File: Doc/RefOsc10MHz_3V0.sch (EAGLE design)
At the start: 54 parts, among them CON1 MCX-J-P-X-RA-SM1, CON2 TYCO-AMP_USBUSB-B_SMT, CON3 SD-73100-0105, CON4 AVR-ISP-6SMD, CON5 AVR-JTAG-10SMD, CON6 HEADER-2X3SMD, CON7 MCX-J-P-X-RA-SM1, IC11 712-RXM-GNSS-TM-B, IC3 74HCT221D, IC4 CFPT-141

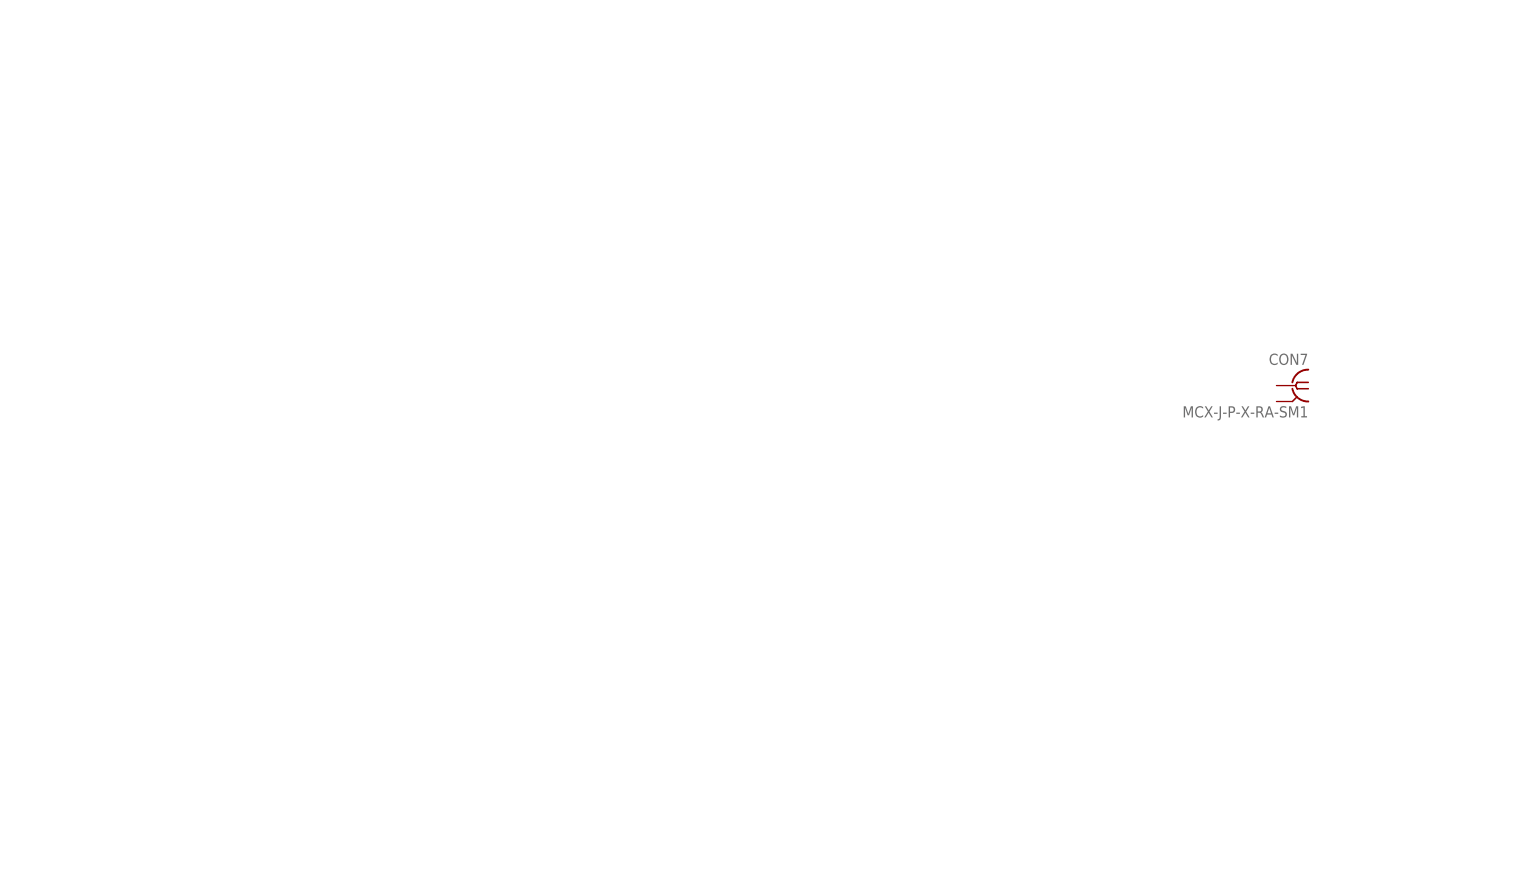
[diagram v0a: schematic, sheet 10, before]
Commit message: avr_DF4IAH_Bootloader - Doc - Eagle: V3.0 - REAR panel connected
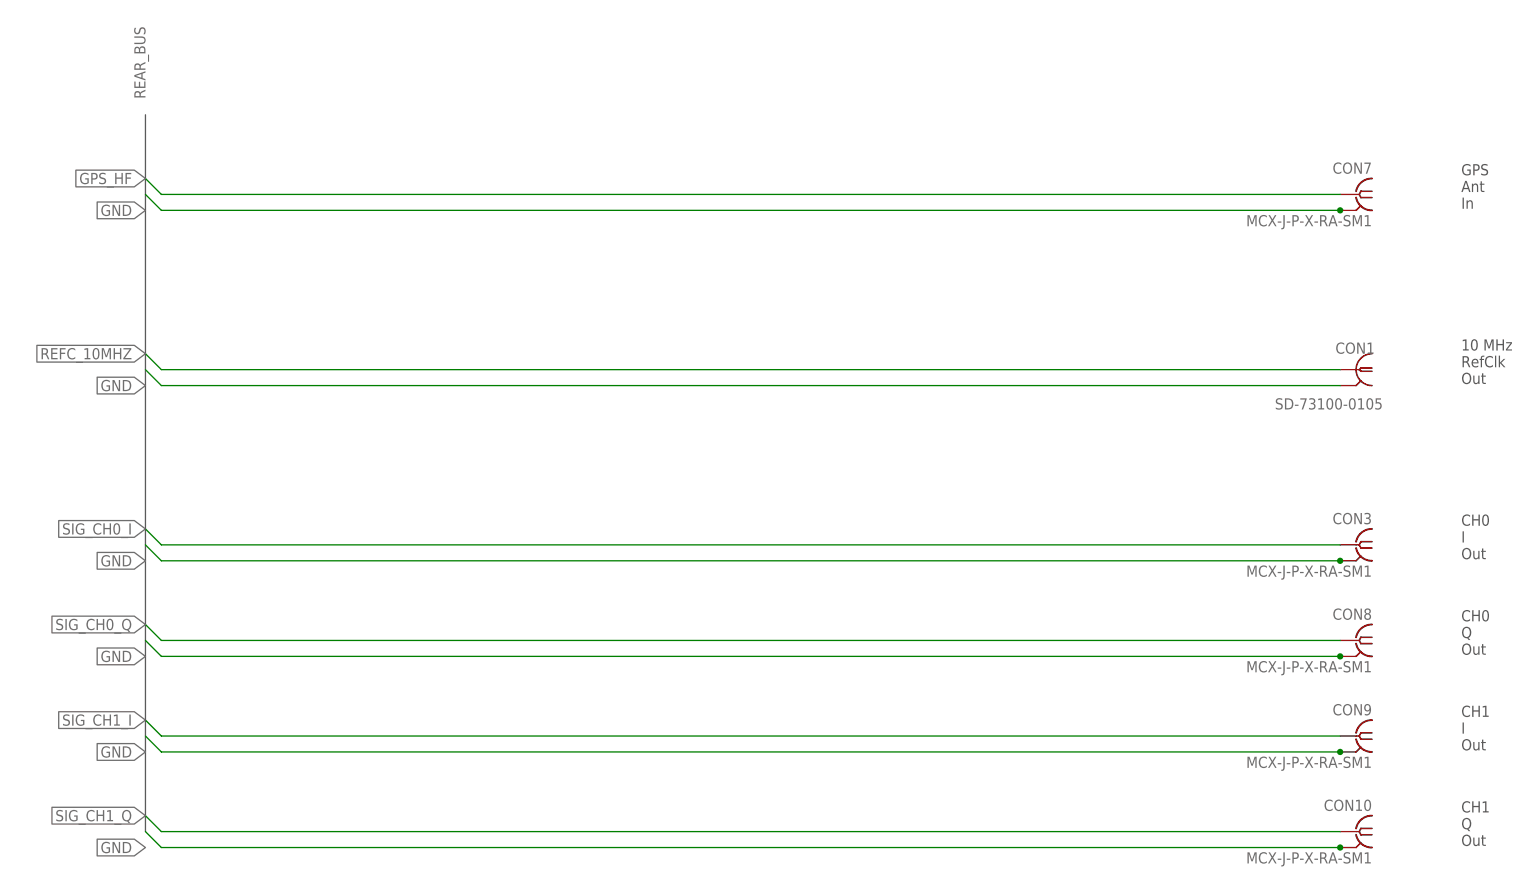
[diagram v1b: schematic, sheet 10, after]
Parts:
- removed R61: 51, rcl:R-EU_R0805
- added CON10, CON8, CON9: MCX-J-P-X-RA-SM1, df4iah:MCX-J-P-X-RA-SM1
- added R10: 51, rcl:R-EU_R0805
- CON1: value MCX-J-P-X-RA-SM1 -> SD-73100-0105; device df4iah:MCX-J-P-X-RA-SM1 -> df4iah:MOLEX_BNC-JACK-50R_SD-73100-0105
- CON3: value SD-73100-0105 -> MCX-J-P-X-RA-SM1; device df4iah:MOLEX_BNC-JACK-50R_SD-73100-0105 -> df4iah:MCX-J-P-X-RA-SM1
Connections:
- removed net C_10MHZ: R61.1
- removed net N$42: CON3.1, R61.2
- new net REFC_10MHZ: CON1.1
- new net SIG_CH0_I: CON3.1
- new net SIG_CH0_Q: CON8.1
- new net SIG_CH1_I: CON9.1
- new net SIG_CH1_Q: CON10.1
- net GND: now also CON1.2, CON1.3, CON10.2, CON10.3, CON10.4, CON10.5, CON3.4, CON3.5, CON7.2, CON7.3, CON7.4, CON7.5, CON8.2, CON8.3, CON8.4, CON8.5, CON9.2, CON9.3, CON9.4, CON9.5
- net GPS_HF: now also CON7.1
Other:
- note added: "CH0 I Out"
- note added: "CH0 Q Out"
- note added: "CH1 I Out"
- note added: "CH1 Q Out"
- note added: "GPS Ant In"
- moved on the sheet: CON7

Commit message: avr_DF4IAH_Bootloader - Doc - Eagle: V3.0 - FPGA and MMU, first attempt, added
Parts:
- added IC1: XMEGA128A1, atmel:XMEGA128A1
- added R1: 200, rcl:R-EU_R0805
- added U1: 6SLX4TQG144, xilinx_devices_V6:6SLX4TQG144
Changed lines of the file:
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@@
 <setting verticaltext="up"/>
 </settings>
-<grid distance="0.1" unitdist="inch" unit="mm" style="lines" multiple="1" display="yes" altdistance="0.01" altunitdist="inch" altunit="mm"/>
+<grid distance="0.1" unitdist="inch" unit="inch" style="lines" multiple="1" display="yes" altdistance="0.01" altunitdist="inch" altunit="inch"/>
 <layers>
 <layer number="1" name="Top" color="4" fill="1" visible="no" active="no"/>
@@
 <part name="CON10" library="df4iah" deviceset="MCX-J-P-X-RA-SM1" device=""/>
 <part name="R10" library="rcl" deviceset="R-EU_" device="R0805" value="51"/>
+<part name="U1" library="xilinx_devices_V6" deviceset="6SLX4TQG144" device=""/>
+<part name="FRAME10" library="frames" deviceset="A5L-LOC" device=""/>
+<part name="FRAME12" library="frames" deviceset="A5L-LOC" device=""/>
+<part name="FRAME13" library="frames" deviceset="A5L-LOC" device=""/>
+<part name="FRAME14" library="frames" deviceset="A5L-LOC" device=""/>
+<part name="FRAME15" library="frames" deviceset="A5L-LOC" device=""/>
+<part name="R1" library="rcl" deviceset="R-EU_" device="R0805" value="200"/>
+<part name="IC1" library="atmel" deviceset="XMEGA128A1" device=""/>
 </parts>
 <sheets>
@@
 <instances>
 <instance part="FRAME2" gate="G$1" x="0" y="7.62"/>
-</instances>
-<busses>
-</busses>
-<nets>
-</nets>
-</sheet>
-<sheet>
-<description>FPGA</description>
+<instance part="R1" gate="G$1" x="213.36" y="137.16"/>
+<instance part="IC1" gate="G$1" x="96.52" y="99.06"/>
+</instances>
+<busses>
+</busses>
+<nets>
+</nets>
+</sheet>
+<sheet>
+<description>FPGA_B1</description>
 <plain>
 </plain>
 <instances>
 <instance part="FRAME3" gate="G$1" x="0" y="7.62"/>
-<instance part="R10" gate="G$1" x="231.14" y="109.22" rot="R180"/>
-</instances>
-<busses>
+<instance part="R10" gate="G$1" x="238.76" y="116.84"/>
+<instance part="U1" gate="B0" x="33.02" y="137.16"/>
+<instance part="U1" gate="B1" x="33.02" y="53.34"/>
+<instance part="U1" gate="B2" x="129.54" y="137.16"/>
+<instance part="U1" gate="B3" x="129.54" y="53.34"/>
+<instance part="U1" gate="BGND" x="205.74" y="160.02"/>
+<instance part="U1" gate="BNA" x="205.74" y="83.82"/>
+<instance part="U1" gate="BVCCAUX" x="205.74" y="55.88"/>
+<instance part="U1" gate="BVCCINT" x="241.3" y="83.82"/>
+</instances>
+<busses>
+</busses>
+<nets>
+</nets>
+</sheet>
+<sheet>
+<description>FPGA_B2</description>
+<plain>
+</plain>
+<instances>
+<instance part="FRAME10" gate="G$1" x="0" y="7.62"/>
+</instances>
+<busses>
+</busses>
+<nets>
+</nets>
+</sheet>
+<sheet>
+<description>FPGA_B3</description>
+<plain>
+</plain>
+<instances>
+<instance part="FRAME12" gate="G$1" x="0" y="7.62"/>
+</instances>
+<busses>
+</busses>
+<nets>
+</nets>
+</sheet>
+<sheet>
+<description>FPGA_B4</description>
+<plain>
+</plain>
+<instances>
+<instance part="FRAME13" gate="G$1" x="0" y="7.62"/>
+</instances>
+<busses>
+</busses>
+<nets>
+</nets>
+</sheet>
+<sheet>
+<description>FPGA_JTAG</description>
+<plain>
+</plain>
+<instances>
+<instance part="FRAME14" gate="G$1" x="0" y="7.62"/>
+</instances>
+<busses>
+</busses>
+<nets>
+</nets>
+</sheet>
+<sheet>
+<description>FPGA_PWR</description>
+<plain>
+</plain>
+<instances>
+<instance part="FRAME15" gate="G$1" x="0" y="7.62"/>
+</instances>
+<busses>

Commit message: avr_DF4IAH_Bootloader - Doc - Eagle: V3.0 - MMU (AVR ATmega) moved into FPGA using a free MMU core from opencores.org.
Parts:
- removed IC1: XMEGA128A1, atmel:XMEGA128A1
- removed R1: 200, rcl:R-EU_R0805
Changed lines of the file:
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@@
 <?xml version="1.0" encoding="utf-8"?>
 <!DOCTYPE eagle SYSTEM "eagle.dtd">
-<eagle version="6.5.0">
+<eagle version="7.2.0">
 <drawing>
 <settings>
@@
 <setting verticaltext="up"/>
 </settings>
-<grid distance="0.1" unitdist="inch" unit="inch" style="lines" multiple="1" display="yes" altdistance="0.01" altunitdist="inch" altunit="inch"/>
+<grid distance="0.1" unitdist="inch" unit="inch" style="lines" multiple="1" display="no" altdistance="0.01" altunitdist="inch" altunit="inch"/>
 <layers>
 <layer number="1" name="Top" color="4" fill="1" visible="no" active="no"/>
@@
 <part name="CON4" library="atmel-1" deviceset="AVR-ISP-6" device="SMD"/>
 <part name="FRAME1" library="frames" deviceset="A4L-LOC" device=""/>
-<part name="FRAME2" library="frames" deviceset="A4L-LOC" device=""/>
 <part name="FRAME3" library="frames" deviceset="A4L-LOC" device=""/>
 <part name="FRAME4" library="frames" deviceset="A4L-LOC" device=""/>
@@
 <part name="FRAME14" library="frames" deviceset="A5L-LOC" device=""/>
 <part name="FRAME15" library="frames" deviceset="A5L-LOC" device=""/>
-<part name="R1" library="rcl" deviceset="R-EU_" device="R0805" value="200"/>
-<part name="IC1" library="atmel" deviceset="XMEGA128A1" device=""/>
 </parts>
 <sheets>
@@
 <rectangle x1="53.34" y1="157.48" x2="210.82" y2="172.72" layer="90"/>
 <rectangle x1="15.24" y1="157.48" x2="35.56" y2="172.72" layer="90"/>
-<text x="15.24" y="134.62" size="3" layer="95">MMU</text>
 <text x="73.66" y="134.62" size="3" layer="95">VCTCXO</text>
 <text x="111.76" y="134.62" size="3" layer="95">FPGA</text>
@@
 <text x="76.2" y="55.88" size="3" layer="95">PMU</text>
 <rectangle x1="233.68" y1="38.1" x2="246.38" y2="132.08" layer="90"/>
-<rectangle x1="15.24" y1="106.68" x2="35.56" y2="132.08" layer="90"/>
-<rectangle x1="111.76" y1="106.68" x2="132.08" y2="132.08" layer="90"/>
+<rectangle x1="111.76" y1="106.68" x2="142.24" y2="132.08" layer="90"/>
 <rectangle x1="190.5" y1="106.68" x2="210.82" y2="132.08" layer="90"/>
 <rectangle x1="76.2" y1="27.94" x2="96.52" y2="53.34" layer="90"/>
 <rectangle x1="15.24" y1="27.94" x2="35.56" y2="53.34" layer="90"/>
+<wire x1="124.46" y1="129.54" x2="124.46" y2="109.22" width="0.1524" layer="94"/>
+<wire x1="124.46" y1="109.22" x2="114.3" y2="109.22" width="0.1524" layer="94"/>
+<wire x1="114.3" y1="109.22" x2="114.3" y2="129.54" width="0.1524" layer="94"/>
+<wire x1="114.3" y1="129.54" x2="124.46" y2="129.54" width="0.1524" layer="94"/>
+<text x="116.84" y="119.38" size="1.778" layer="94">MMU</text>
 </plain>
 <instances>
@@
 <bus name="USB_BUS">
 <segment>
-<wire x1="30.48" y1="53.34" x2="30.48" y2="106.68" width="0.1524" layer="92"/>
+<wire x1="30.48" y1="53.34" x2="30.48" y2="104.14" width="0.1524" layer="92"/>
 <label x="27.94" y="71.12" size="1.778" layer="95" rot="R270"/>
+<wire x1="30.48" y1="104.14" x2="114.3" y2="104.14" width="0.1524" layer="92"/>
+<wire x1="114.3" y1="104.14" x2="114.3" y2="106.68" width="0.1524" layer="92"/>
+<label x="61.214" y="105.41" size="1.778" layer="95"/>
 </segment>
 </bus>
@@
 <wire x1="96.52" y1="38.1" x2="111.76" y2="38.1" width="0.1524" layer="92"/>
 <wire x1="111.76" y1="38.1" x2="111.76" y2="99.06" width="0.1524" layer="92"/>
-<wire x1="111.76" y1="99.06" x2="20.32" y2="99.06" width="0.1524" layer="92"/>
 <wire x1="111.76" y1="99.06" x2="198.12" y2="99.06" width="0.1524" layer="92"/>
 <label x="109.22" y="73.66" size="1.778" layer="95" rot="R270"/>
-<label x="52.578" y="101.6" size="1.778" layer="95" rot="R180"/>
+<label x="168.402" y="100.076" size="1.778" layer="95"/>
 </segment>
 </bus>
 <bus name="GPS_BUS">
 <segment>
-<wire x1="30.48" y1="132.08" x2="30.48" y2="142.24" width="0.1524" layer="92"/>
-<wire x1="30.48" y1="142.24" x2="127" y2="142.24" width="0.1524" layer="92"/>
 <wire x1="127" y1="142.24" x2="205.74" y2="142.24" width="0.1524" layer="92"/>
 <wire x1="205.74" y1="142.24" x2="205.74" y2="132.08" width="0.1524" layer="92"/>
 <label x="205.74" y="144.78" size="1.778" layer="95" rot="R180"/>
 <wire x1="127" y1="142.24" x2="127" y2="132.08" width="0.1524" layer="92"/>
-<label x="40.64" y="144.78" size="1.778" layer="95" rot="R180"/>
 </segment>
 </bus>
 <bus name="REAR_BUS">
 <segment>
-<wire x1="132.08" y1="111.76" x2="137.16" y2="111.76" width="0.1524" layer="92"/>
-<wire x1="137.16" y1="111.76" x2="137.16" y2="58.42" width="0.1524" layer="92"/>
-<wire x1="137.16" y1="58.42" x2="215.9" y2="58.42" width="0.1524" layer="92"/>
+<wire x1="142.24" y1="111.76" x2="144.78" y2="111.76" width="0.1524" layer="92"/>
+<wire x1="144.78" y1="111.76" x2="144.78" y2="58.42" width="0.1524" layer="92"/>
+<wire x1="144.78" y1="58.42" x2="215.9" y2="58.42" width="0.1524" layer="92"/>
 <label x="231.14" y="60.96" size="1.778" layer="95" rot="R180"/>
 <wire x1="215.9" y1="58.42" x2="233.68" y2="58.42" width="0.1524" layer="92"/>
@@
 <bus name="MMU_BUS">
 <segment>
-<wire x1="35.56" y1="109.22" x2="55.88" y2="109.22" width="0.1524" layer="92"/>
-<label x="50.8" y="111.76" size="1.778" layer="95" rot="R180"/>
+<label x="60.96" y="110.49" size="1.778" layer="95"/>
 <wire x1="55.88" y1="109.22" x2="111.76" y2="109.22" width="0.1524" layer="92"/>
 <wire x1="55.88" y1="109.22" x2="55.88" y2="152.4" width="0.1524" layer="92"/>
@@
 <net name="PWR_3V3" class="2">
 <segment>
-<wire x1="20.32" y1="99.06" x2="17.78" y2="101.6" width="0.1524" layer="91"/>
-<wire x1="17.78" y1="101.6" x2="17.78" y2="106.68" width="0.1524" layer="91"/>
-<label x="20.32" y="99.06" size="1.778" layer="95" rot="R270" xref="yes"/>
-</segment>
-<segment>
 <wire x1="116.84" y1="99.06" x2="119.38" y2="101.6" width="0.1524" layer="91"/>
 <wire x1="119.38" y1="101.6" x2="119.38" y2="106.68" width="0.1524" layer="91"/>
@@
 <wire x1="86.36" y1="119.38" x2="86.36" y2="114.3" width="0.1524" layer="91"/>
 <wire x1="86.36" y1="114.3" x2="111.76" y2="114.3" width="0.1524" layer="91"/>
-<wire x1="86.36" y1="114.3" x2="35.56" y2="114.3" width="0.1524" layer="91"/>
-<junction x="86.36" y="114.3"/>
-<label x="101.6" y="116.84" size="1.778" layer="95" rot="R180"/>
+<label x="91.186" y="115.062" size="1.778" layer="95"/>
 </segment>
 </net>
 <net name="VCTCXO_VC" class="0">
 <segment>
-<wire x1="35.56" y1="127" x2="76.2" y2="127" width="0.1524" layer="91"/>
-<label x="73.66" y="129.54" size="1.778" layer="95" rot="R180"/>
+<wire x1="88.9" y1="127" x2="111.76" y2="127" width="0.1524" layer="91"/>
+<label x="90.932" y="128.016" size="1.778" layer="95"/>
 </segment>
 </net>
@@
 </nets>
 </sheet>
-<sheet>
-<description>MMU</description>
-<plain>
-</plain>
-<instances>
-<instance part="FRAME2" gate="G$1" x="0" y="7.62"/>
-<instance part="R1" gate="G$1" x="213.36" y="137.16"/>
-<instance part="IC1" gate="G$1" x="96.52" y="99.06"/>
-</instances>
-<busses>
-</busses>
-<nets>
-</nets>
-</sheet>
